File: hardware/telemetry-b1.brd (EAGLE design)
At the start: 63.5 x 76.2 mm, 117 parts, among them IC1 COPERNICUSSMD, IC10 TPS70933, IC2 TPS70933, IC4 STM32L073CZT6, IC5 TPS62160, IC6 HX1, IC7 LMP7702, J1 I2C, J10 TEMP_BAT, J11 DNP, J12 INSOL, J13 SMA_EDGE, J3 SMA_EDGE, J4 USD-SOCKET, J5 BAT, J6 SMA_EDGE, J7 SMA_EDGE, J8 TEMP_GPS, J9 TEMP_HOT, K1 ARE104H, K2 ARE104H, Q1 AO3400A, Q2 AO3400A, U1 LTC3105, U2 INA219, Y1 32768, Y2 8M

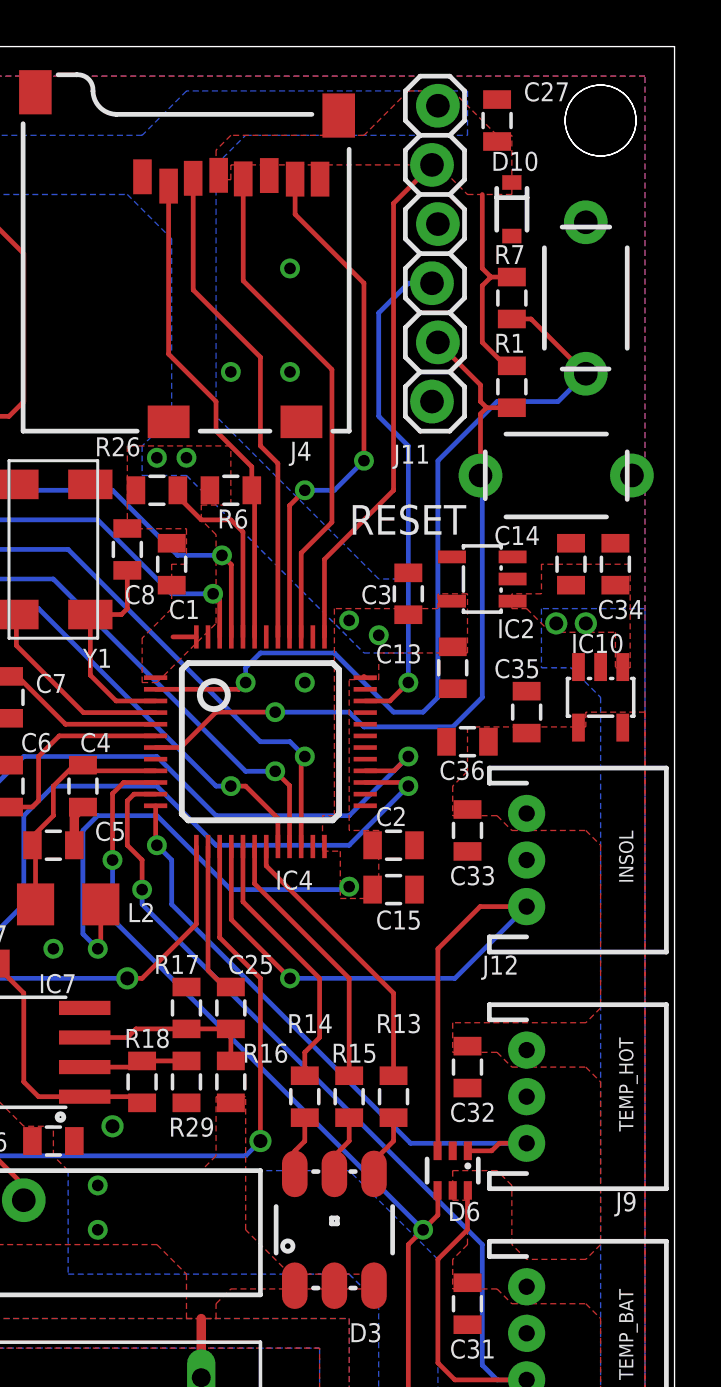
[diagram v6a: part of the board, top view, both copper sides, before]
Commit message: Swap HXEN pin to 5VT pin
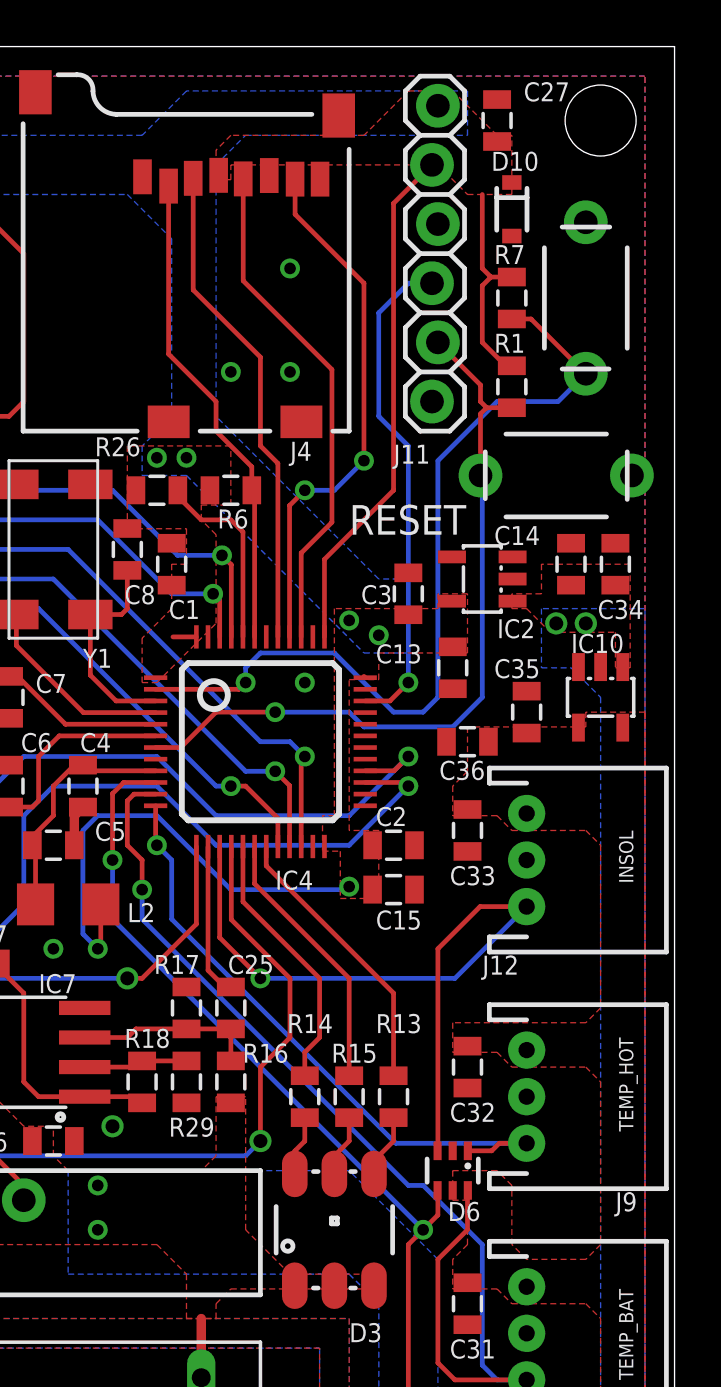
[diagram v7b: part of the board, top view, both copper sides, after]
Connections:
- net HXEN: now also IC4.16; no longer IC4.15
- net INSOL: now also IC4.15; no longer IC4.16
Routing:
- net INSOL: track 31.4 -> 32.3 mm
- net HXEN: track 39.3 -> 40.1 mm
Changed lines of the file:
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@@
 <layer number="25" name="tNames" color="7" fill="1" visible="yes" active="yes"/>
 <layer number="26" name="bNames" color="7" fill="1" visible="yes" active="yes"/>
-<layer number="27" name="tValues" color="7" fill="1" visible="no" active="yes"/>
-<layer number="28" name="bValues" color="7" fill="1" visible="no" active="yes"/>
+<layer number="27" name="tValues" color="7" fill="1" visible="yes" active="yes"/>
+<layer number="28" name="bValues" color="7" fill="1" visible="yes" active="yes"/>
 <layer number="29" name="tStop" color="7" fill="3" visible="no" active="yes"/>
 <layer number="30" name="bStop" color="7" fill="6" visible="no" active="yes"/>
@@
 <text x="27.94" y="60.325" size="1.27" layer="22" ratio="10" rot="MR0">HAB Project</text>
 <text x="31.115" y="58.42" size="1.27" layer="22" ratio="10" rot="MR0">Telemetry Rev 3B</text>
-<hole x="60.325" y="73.025" drill="3.048"/>
 </plain>
 <attributes>
@@
 <wire x1="54.61" y1="27.075" x2="54.625" y2="27.09" width="0.2032" layer="1"/>
 <via x="40.64" y="40.005" extent="1-16" drill="0.5"/>
-<wire x1="40.64" y1="40.005" x2="40.64" y2="39.37" width="0.2032" layer="16"/>
-<wire x1="40.64" y1="39.37" x2="55.245" y2="24.765" width="0.2032" layer="16"/>
+<wire x1="40.64" y1="40.005" x2="40.64" y2="38.735" width="0.2032" layer="16"/>
+<wire x1="40.64" y1="38.735" x2="52.07" y2="27.305" width="0.2032" layer="16"/>
+<wire x1="52.07" y1="27.305" x2="52.705" y2="27.305" width="0.2032" layer="16"/>
+<wire x1="52.705" y1="27.305" x2="55.245" y2="24.765" width="0.2032" layer="16"/>
 <wire x1="55.245" y1="24.765" x2="55.245" y2="19.59" width="0.2032" layer="16"/>
 <wire x1="55.245" y1="19.59" x2="55.88" y2="18.955" width="0.2032" layer="16"/>
@@
 <contactref element="IC6" pad="4"/>
 <contactref element="R23" pad="1"/>
-<contactref element="IC4" pad="15"/>
-<wire x1="43.97" y1="41.855" x2="43.97" y2="37.945" width="0.2032" layer="1"/>
-<wire x1="43.97" y1="37.945" x2="45.72" y2="36.195" width="0.2032" layer="1"/>
-<wire x1="45.72" y1="36.195" x2="45.72" y2="29.21" width="0.2032" layer="1"/>
+<wire x1="46.99" y1="36.195" x2="46.99" y2="33.655" width="0.2032" layer="1"/>
+<wire x1="46.99" y1="33.655" x2="45.72" y2="32.385" width="0.2032" layer="1"/>
+<wire x1="45.72" y1="32.385" x2="45.72" y2="29.21" width="0.2032" layer="1"/>
 <wire x1="45.72" y1="29.21" x2="45.085" y2="28.575" width="0.2032" layer="16"/>
 <wire x1="45.085" y1="28.575" x2="28.575" y2="28.575" width="0.2032" layer="16"/>
@@
 <wire x1="23.23" y1="28.205" x2="24.765" y2="26.67" width="0.2032" layer="1"/>
 <wire x1="24.765" y1="26.67" x2="27.94" y2="26.67" width="0.2032" layer="1"/>
+<contactref element="IC4" pad="16"/>
+<wire x1="44.47" y1="41.855" x2="44.47" y2="38.715" width="0.2032" layer="1"/>
+<wire x1="44.47" y1="38.715" x2="46.99" y2="36.195" width="0.2032" layer="1"/>
 </signal>
 <signal name="RC">
@@
 <contactref element="J12" pad="3"/>
 <contactref element="D6" pad="3"/>
-<contactref element="IC4" pad="16"/>
 <wire x1="57.15" y1="39.275" x2="55.15" y2="39.275" width="0.2032" layer="1"/>
 <wire x1="55.15" y1="39.275" x2="53.34" y2="37.465" width="0.2032" layer="1"/>
 <wire x1="53.34" y1="37.465" x2="53.34" y2="28.805" width="0.2032" layer="1"/>
 <wire x1="53.34" y1="28.805" x2="53.325" y2="28.79" width="0.2032" layer="1"/>
-<via x="46.99" y="36.195" extent="1-16" drill="0.5"/>
-<wire x1="44.47" y1="41.855" x2="44.47" y2="38.715" width="0.2032" layer="1"/>
-<wire x1="44.47" y1="38.715" x2="46.99" y2="36.195" width="0.2032" layer="1"/>
-<wire x1="46.99" y1="36.195" x2="54.07" y2="36.195" width="0.2032" layer="16"/>
+<via x="45.72" y="36.195" extent="1-16" drill="0.5"/>
+<wire x1="45.72" y1="36.195" x2="54.07" y2="36.195" width="0.2032" layer="16"/>
 <wire x1="54.07" y1="36.195" x2="57.15" y2="39.275" width="0.2032" layer="16"/>
+<contactref element="IC4" pad="15"/>
+<wire x1="43.97" y1="41.855" x2="43.97" y2="37.945" width="0.2032" layer="1"/>
+<wire x1="43.97" y1="37.945" x2="45.72" y2="36.195" width="0.2032" layer="1"/>
 </signal>
 <signal name="VS">
@@
 <via x="41.275" y="41.91" extent="1-16" drill="0.5"/>
 <wire x1="41.275" y1="41.91" x2="41.91" y2="41.275" width="0.2032" layer="16"/>
-<wire x1="41.91" y1="41.275" x2="41.91" y2="39.37" width="0.2032" layer="16"/>
-<wire x1="41.91" y1="39.37" x2="52.165" y2="29.115" width="0.2032" layer="16"/>
-<wire x1="57.15" y1="29.115" x2="52.165" y2="29.115" width="0.2032" layer="16"/>
+<wire x1="41.91" y1="41.275" x2="41.91" y2="38.735" width="0.2032" layer="16"/>
+<wire x1="41.91" y1="38.735" x2="51.53" y2="29.115" width="0.2032" layer="16"/>
+<wire x1="57.15" y1="29.115" x2="51.53" y2="29.115" width="0.2032" layer="16"/>
 <wire x1="41.22" y1="43.605" x2="41.22" y2="41.965" width="0.2032" layer="1"/>
 <wire x1="41.22" y1="41.965" x2="41.275" y2="41.91" width="0.2032" layer="1"/>

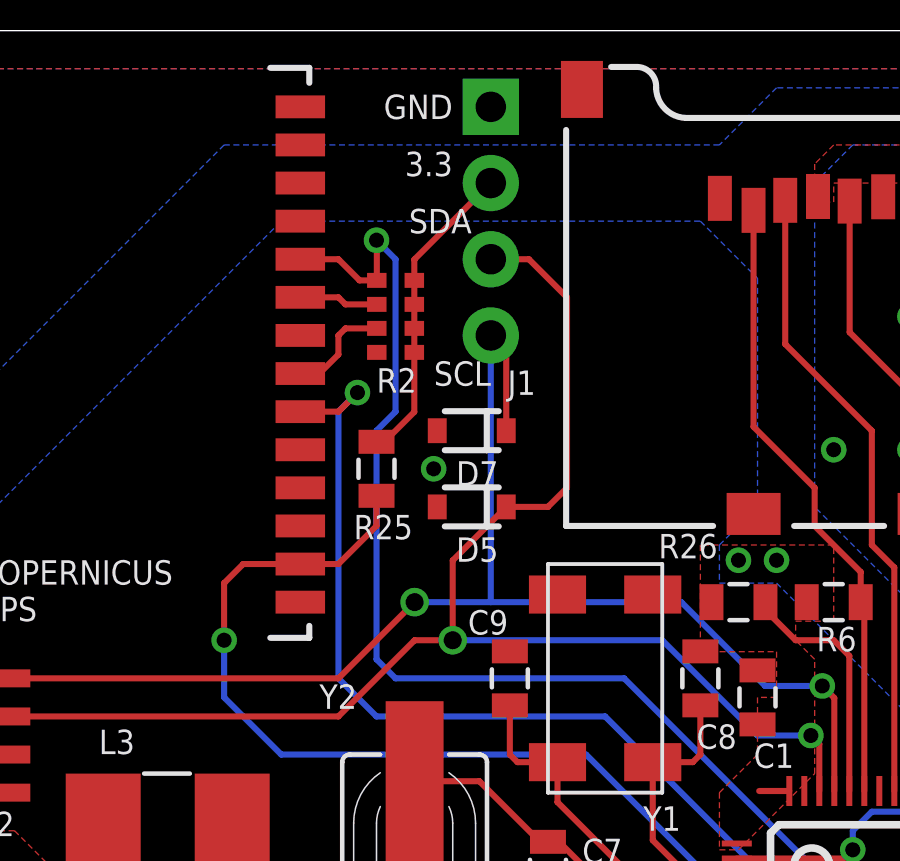
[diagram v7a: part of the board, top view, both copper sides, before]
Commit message: Fix I2C pull-up resistors in beta/regular boards; add Phoenix board and some datasheets
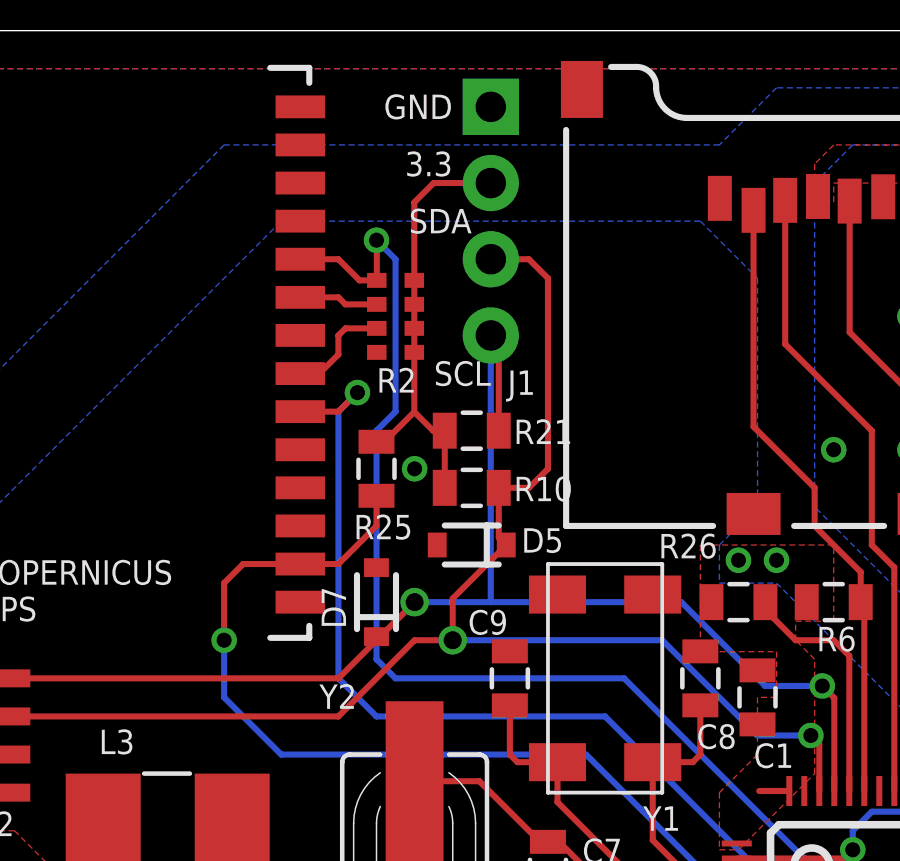
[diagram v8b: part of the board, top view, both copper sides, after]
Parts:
- added R10, R21: 4.7K, SparkFun-Passives:0805
- moved D7 6.54 mm to (29.2, 57.1), turned to 90 degrees
- moved D5 1.27 mm to (32.4, 59.1)
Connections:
- net 3.3V: now also R10.1, R21.1
- net SCL: now also R21.2
- net SDA: now also R10.2
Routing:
- net 3.3V: track 41.1 -> 45.4 mm
- net SDA: track 48.3 -> 47.8 mm
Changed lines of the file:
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@@
 ~STCARLSO
 301 956 5041</text>
-<text x="34.29" y="62.23" size="1.27" layer="22" ratio="10" rot="MR0">Microsoft Maker Garage</text>
-<text x="27.94" y="60.325" size="1.27" layer="22" ratio="10" rot="MR0">HAB Project</text>
-<text x="31.115" y="58.42" size="1.27" layer="22" ratio="10" rot="MR0">Telemetry Rev 3B</text>
+<text x="31.75" y="62.23" size="1.27" layer="22" ratio="10" rot="MR0">Microsoft Maker Garage</text>
+<text x="25.4" y="60.325" size="1.27" layer="22" ratio="10" rot="MR0">HAB Project</text>
+<text x="28.575" y="58.42" size="1.27" layer="22" ratio="10" rot="MR0">Telemetry Rev 3B</text>
 </plain>
 <attributes>
@@
 <attribute name="NAME" x="21.209" y="28.829" size="0.8128" layer="25" rot="R180"/>
 </element>
-<element name="D5" library="SparkFun-DiscreteSemi" package="SOD-323" value="5.6V" x="32.385" y="60.325" smashed="yes" rot="R180">
-<attribute name="PROD_ID" value="DIO-12442" x="32.385" y="60.325" size="1.778" layer="27" rot="R180" display="off"/>
-<attribute name="NAME" x="33.274" y="59.309" size="0.8128" layer="25" rot="R180"/>
+<element name="D5" library="SparkFun-DiscreteSemi" package="SOD-323" value="5.6V" x="32.385" y="59.055" smashed="yes" rot="R180">
+<attribute name="PROD_ID" value="DIO-12442" x="32.385" y="59.055" size="1.778" layer="27" rot="R180" display="off"/>
+<attribute name="NAME" x="34.036" y="58.801" size="0.8128" layer="25"/>
 </element>
 <element name="D6" library="HAB" package="SC70-6L" value="CM1213A" x="53.975" y="27.94" smashed="yes" rot="R180">
@@
 <attribute name="VALUE" x="59.62" y="26.48" size="0.6096" layer="27" rot="R180"/>
 </element>
-<element name="D7" library="SparkFun-DiscreteSemi" package="SOD-323" value="5.6V" x="32.385" y="62.865" smashed="yes" rot="R180">
-<attribute name="PROD_ID" value="DIO-12442" x="32.385" y="62.865" size="1.778" layer="27" rot="R180" display="off"/>
-<attribute name="NAME" x="33.274" y="61.849" size="0.8128" layer="25" rot="R180"/>
+<element name="D7" library="SparkFun-DiscreteSemi" package="SOD-323" value="5.6V" x="29.21" y="57.15" smashed="yes" rot="R90">
+<attribute name="PROD_ID" value="DIO-12442" x="29.21" y="57.15" size="1.778" layer="27" rot="R90" display="off"/>
+<attribute name="NAME" x="28.194" y="56.261" size="0.8128" layer="25" rot="R90"/>
 </element>
 <element name="D8" library="SparkFun-DiscreteSemi" package="SOD-323" value="BAT20J" x="8.89" y="33.02" smashed="yes" rot="R270">
@@
 <element name="U$2" library="HAB" package="GARAGE" value="" x="20.955" y="68.58" smashed="yes" rot="MR0"/>
 <element name="U$5" library="HAB" package="MSFT_LOGO" value="" x="20.32" y="16.51" smashed="yes" rot="MR0"/>
+<element name="R21" library="SparkFun-Passives" package="0805" value="4.7K" x="32.385" y="62.865" smashed="yes">
+<attribute name="NAME" x="33.782" y="62.4205" size="0.8128" layer="25"/>
+<attribute name="VALUE" x="31.369" y="63.373" size="0.6096" layer="27"/>
+</element>
+<element name="R10" library="SparkFun-Passives" package="0805" value="4.7K" x="32.385" y="60.96" smashed="yes">
+<attribute name="NAME" x="33.782" y="60.5155" size="0.8128" layer="25"/>
+<attribute name="VALUE" x="31.369" y="61.468" size="0.6096" layer="27"/>
+</element>
 </elements>
 <signals>
@@
 <via x="47.625" y="48.895" extent="1-16" drill="0.5"/>
 <via x="46.99" y="66.675" extent="1-16" drill="0.5"/>
-<via x="31.115" y="61.595" extent="1-16" drill="0.5"/>
+<via x="30.48" y="61.595" extent="1-16" drill="0.5"/>
 <via x="44.45" y="62.23" extent="1-16" drill="0.5"/>
 <via x="36.83" y="37.465" extent="1-16" drill="0.5"/>
@@
 <wire x1="55.245" y1="65.935" x2="55.615" y2="66.305" width="0.2032" layer="1"/>
 <via x="49.53" y="40.132" extent="1-16" drill="0.5"/>
-<wire x1="30.47" y1="67.875" x2="30.47" y2="68.57" width="0.2032" layer="1"/>
-<wire x1="30.47" y1="68.57" x2="33.02" y2="71.12" width="0.2032" layer="1"/>
 <wire x1="30.47" y1="65.475" x2="30.47" y2="63.49" width="0.2032" layer="1"/>
 <wire x1="29.21" y1="62.495" x2="29.475" y2="62.495" width="0.2032" layer="1"/>
@@
 <wire x1="49.403" y1="40.005" x2="49.53" y2="40.132" width="0.2032" layer="16"/>
 <wire x1="38.865" y1="37.595" x2="38.735" y2="37.465" width="0.2032" layer="1"/>
+<contactref element="R21" pad="1"/>
+<contactref element="R10" pad="1"/>
+<wire x1="30.47" y1="67.875" x2="30.47" y2="70.475" width="0.2032" layer="1"/>
+<wire x1="30.47" y1="70.475" x2="31.115" y2="71.12" width="0.2032" layer="1"/>
+<wire x1="31.115" y1="71.12" x2="33.02" y2="71.12" width="0.2032" layer="1"/>
+<wire x1="31.485" y1="62.865" x2="31.095" y2="62.865" width="0.2032" layer="1"/>
+<wire x1="31.095" y1="62.865" x2="30.47" y2="63.49" width="0.2032" layer="1"/>
+<wire x1="31.485" y1="60.96" x2="31.485" y2="62.865" width="0.2032" layer="1"/>
 </signal>
 <signal name="VDDA">
@@
 <via x="44.069" y="54.356" extent="1-16" drill="0.5"/>
 <wire x1="16.57" y1="54.61" x2="27.94" y2="54.61" width="0.2032" layer="1"/>
-<wire x1="27.94" y1="54.61" x2="30.48" y2="57.15" width="0.2032" layer="1"/>
 <via x="30.48" y="57.15" extent="1-16" drill="0.6"/>
 <wire x1="30.48" y1="57.15" x2="33.02" y2="57.15" width="0.2032" layer="16"/>
@@
 <wire x1="44.069" y1="54.356" x2="42.164" y2="54.356" width="0.2032" layer="16"/>
 <wire x1="42.164" y1="54.356" x2="39.37" y2="57.15" width="0.2032" layer="16"/>
-<wire x1="33.535" y1="62.865" x2="33.535" y2="65.525" width="0.2032" layer="1"/>
 <wire x1="33.02" y1="66.04" x2="33.02" y2="57.15" width="0.2032" layer="16"/>
-<wire x1="33.535" y1="65.525" x2="33.02" y2="66.04" width="0.2032" layer="1"/>
+<contactref element="R21" pad="2"/>
+<wire x1="33.285" y1="62.865" x2="33.285" y2="65.775" width="0.2032" layer="1"/>
+<wire x1="33.285" y1="65.775" x2="33.02" y2="66.04" width="0.2032" layer="1"/>
+<wire x1="29.21" y1="56" x2="29.33" y2="56" width="0.2032" layer="1"/>
+<wire x1="29.33" y1="56" x2="30.48" y2="57.15" width="0.2032" layer="1"/>
+<wire x1="29.21" y1="56" x2="29.21" y2="55.88" width="0.2032" layer="1"/>
+<wire x1="29.21" y1="55.88" x2="27.94" y2="54.61" width="0.2032" layer="1"/>
 </signal>
 <signal name="SDA">
@@
 <via x="43.688" y="52.705" extent="1-16" drill="0.5"/>
 <wire x1="16.57" y1="53.34" x2="27.94" y2="53.34" width="0.2032" layer="1"/>
-<wire x1="27.94" y1="53.34" x2="30.48" y2="55.88" width="0.2032" layer="1"/>
 <wire x1="30.48" y1="55.88" x2="31.75" y2="55.88" width="0.2032" layer="1"/>
 <via x="31.75" y="55.88" extent="1-16" drill="0.6"/>
 <wire x1="31.75" y1="55.88" x2="38.735" y2="55.88" width="0.2032" layer="16"/>
-<wire x1="33.535" y1="60.325" x2="34.925" y2="60.325" width="0.2032" layer="1"/>
-<wire x1="34.925" y1="60.325" x2="35.56" y2="60.96" width="0.2032" layer="1"/>
-<wire x1="35.56" y1="60.96" x2="35.56" y2="67.31" width="0.2032" layer="1"/>
-<wire x1="35.56" y1="67.31" x2="34.29" y2="68.58" width="0.2032" layer="1"/>
+<wire x1="34.925" y1="67.945" x2="34.29" y2="68.58" width="0.2032" layer="1"/>
 <wire x1="34.29" y1="68.58" x2="33.02" y2="68.58" width="0.2032" layer="1"/>
-<wire x1="31.75" y1="55.88" x2="31.75" y2="58.54" width="0.2032" layer="1"/>
-<wire x1="31.75" y1="58.54" x2="33.535" y2="60.325" width="0.2032" layer="1"/>
 <wire x1="43.97" y1="50.855" x2="43.97" y2="52.423" width="0.2032" layer="1"/>
 <wire x1="43.97" y1="52.423" x2="43.688" y2="52.705" width="0.2032" layer="1"/>
 <wire x1="38.735" y1="55.88" x2="41.91" y2="52.705" width="0.2032" layer="16"/>
 <wire x1="41.91" y1="52.705" x2="43.688" y2="52.705" width="0.2032" layer="16"/>
+<contactref element="R10" pad="2"/>
+<wire x1="33.285" y1="60.96" x2="34.29" y2="60.96" width="0.2032" layer="1"/>
+<wire x1="34.29" y1="60.96" x2="34.925" y2="61.595" width="0.2032" layer="1"/>
+<wire x1="34.925" y1="61.595" x2="34.925" y2="67.945" width="0.2032" layer="1"/>
+<wire x1="31.75" y1="55.88" x2="31.75" y2="57.27" width="0.2032" layer="1"/>
+<wire x1="31.75" y1="57.27" x2="33.535" y2="59.055" width="0.2032" layer="1"/>
+<wire x1="33.285" y1="60.96" x2="33.285" y2="59.305" width="0.2032" layer="1"/>
+<wire x1="33.285" y1="59.305" x2="33.535" y2="59.055" width="0.2032" layer="1"/>
+<wire x1="27.94" y1="53.34" x2="30.48" y2="55.88" width="0.2032" layer="1"/>
 </signal>
 <signal name="RS0">
